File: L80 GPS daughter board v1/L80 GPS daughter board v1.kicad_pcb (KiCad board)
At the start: 4 copper layers, 29.8 x 35.1 mm, 13 parts, among them J1 Conn_01x06_Socket, SW1 SW_Push, U1 AP2112K-3.3, U2 L80-R, U3 MCP73831-2-OT

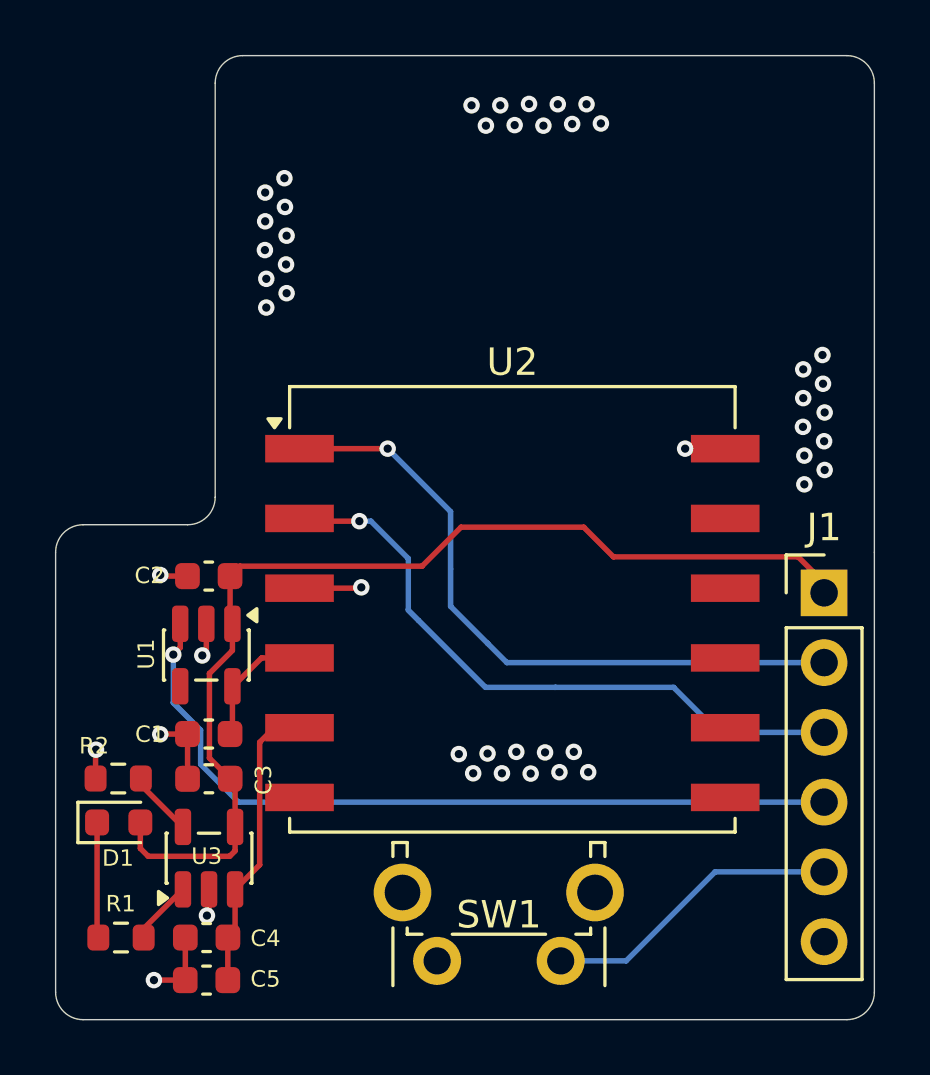
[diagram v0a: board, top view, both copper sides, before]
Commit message: modefied gps board to handle sdcard operations and power input
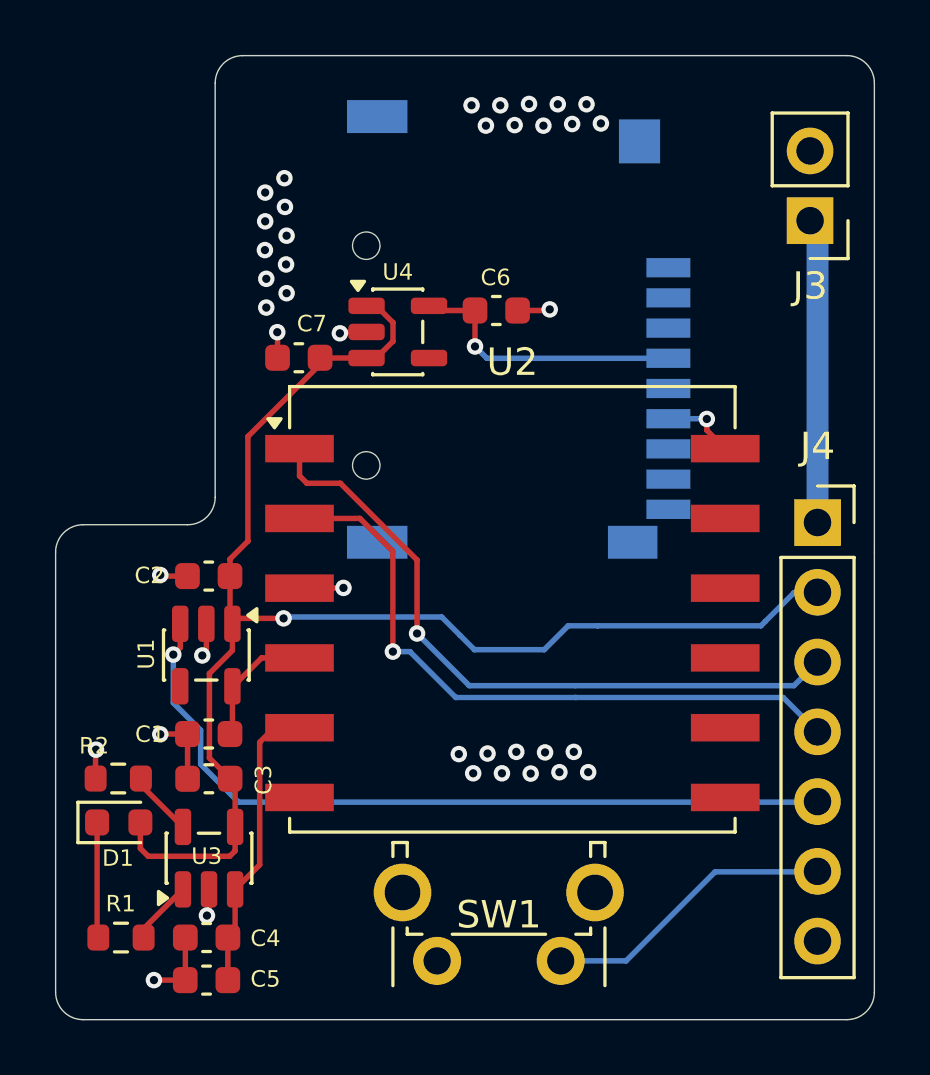
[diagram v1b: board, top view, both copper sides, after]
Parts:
- removed J1: Conn_01x06_Socket, Connector_PinHeader_2.54mm:PinHeader_1x06_P2.54mm_Vertical
- added C6: 1uF, Capacitor_SMD:C_0603_1608Metric, F.Cu at (133.2, 90.1)
- added C7: 1uF, Capacitor_SMD:C_0603_1608Metric, F.Cu at (126.0, 91.8)
- added J2: THD2528-11SD-GF, KiCad:THD252811SDGF, B.Cu at (131.7, 90.5)
- added J3: Conn_01x02_Pin, Connector_PinHeader_2.54mm:PinHeader_1x02_P2.54mm_Vertical, F.Cu at (144.6, 86.8)
- added J4: Conn_01x07_Socket, Connector_PinSocket_2.54mm:PinSocket_1x07_P2.54mm_Vertical, F.Cu at (144.9, 97.8)
- added U4: AP2112K-3.3, Package_TO_SOT_SMD:SOT-23-5, F.Cu at (129.6, 90.8)
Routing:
- net +5V: track 39.1 -> 52.5 mm, vias 0 -> 1
- net 5:32Vin: track 0.00 -> 11.1 mm
- net SD_CARD_PWR: track 0.00 -> 10.3 mm, vias 0 -> 1
- net GND: track 13.3 -> 17.1 mm, vias 48 -> 41
- net gps_tx: track 23.3 -> 24.4 mm
- net gps_rx: track 24.2 -> 24.9 mm

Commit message: added SD card pinout
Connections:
- J2 pad 2: unconnected-(J2-CD/DAT3-Pad2) -> SD_CS
- J2 pad 3: unconnected-(J2-CMD-Pad3) -> MOSI
- J2 pad 5: unconnected-(J2-CLX-Pad5) -> SCLK
- J2 pad 7: unconnected-(J2-DAT0-Pad7) -> MISO
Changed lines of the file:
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@@
 	(net 18 "stat")
 	(net 19 "SD_CARD_PWR")
-	(net 20 "unconnected-(J2-CMD-Pad3)")
+	(net 20 "MOSI")
 	(net 21 "unconnected-(J2-PadMP2)")
 	(net 22 "unconnected-(J2-DAT2-Pad1)")
-	(net 23 "unconnected-(J2-CD{slash}DAT3-Pad2)")
+	(net 23 "SD_CS")
 	(net 24 "unconnected-(J2-PadMP4)")
-	(net 25 "unconnected-(J2-DAT0-Pad7)")
+	(net 25 "MISO")
 	(net 26 "unconnected-(J2-PadMP1)")
 	(net 27 "unconnected-(J2-DAT1-Pad8)")
 	(net 28 "unconnected-(J2-CD-Pad9)")
 	(net 29 "unconnected-(J2-PadMP3)")
-	(net 30 "unconnected-(J2-CLX-Pad5)")
+	(net 30 "SCLK")
 	(net 31 "unconnected-(U4-NC-Pad4)")
 	(net 32 "5:32Vin")
@@
 			(net 22 "unconnected-(J2-DAT2-Pad1)")
 			(pinfunction "DAT2")
-			(pintype "passive")
+			(pintype "passive+no_connect")
 			(teardrops
 				(best_length_ratio 0.5)
@@
 			(size 0.7 1.6)
 			(layers "B.Cu" "B.Mask" "B.Paste")
-			(net 23 "unconnected-(J2-CD{slash}DAT3-Pad2)")
+			(net 23 "SD_CS")
 			(pinfunction "CD/DAT3")
 			(pintype "passive")
@@
 			(size 0.7 1.6)
 			(layers "B.Cu" "B.Mask" "B.Paste")
-			(net 20 "unconnected-(J2-CMD-Pad3)")
+			(net 20 "MOSI")
 			(pinfunction "CMD")
 			(pintype "passive")
@@
 			(size 0.7 1.6)
 			(layers "B.Cu" "B.Mask" "B.Paste")
-			(net 30 "unconnected-(J2-CLX-Pad5)")
+			(net 30 "SCLK")
 			(pinfunction "CLX")
 			(pintype "passive")
@@
 			(size 0.7 1.6)
 			(layers "B.Cu" "B.Mask" "B.Paste")
-			(net 25 "unconnected-(J2-DAT0-Pad7)")
+			(net 25 "MISO")
 			(pinfunction "DAT0")
 			(pintype "passive")
@@
 			(net 27 "unconnected-(J2-DAT1-Pad8)")
 			(pinfunction "DAT1")
-			(pintype "passive")
+			(pintype "passive+no_connect")
 			(teardrops
 				(best_length_ratio 0.5)
@@
 	)
 	(zone
-		(net 19)
-		(net_name "SD_CARD_PWR")
+		(net 5)
+		(net_name "gps_rx")
 		(layer "B.Cu")
 		(name "$teardrop_padvia$")
 		(hatch none 0.1)
-		(priority 30009)
+		(priority 30003)
 		(attr
 			(teardrop
@@
 		(polygon
 			(pts
-				(xy 138.28 91.71) (xy 138.28 91.91) (xy 138.63 92.16) (xy 139.431 91.81) (xy 138.63 91.46)
+				(xy 143.532556 103.63) (xy 143.532556 103.83) (xy 145.025827 103.703667) (xy 144.861 102.87) (xy 144.153251 102.397765)
 			)
 		)
 	)
 	(zone
-		(net 5)
-		(net_name "gps_rx")
+		(net 3)
+		(net_name "+5V")
 		(layer "B.Cu")
 		(name "$teardrop_padvia$")
 		(hatch none 0.1)
-		(priority 30003)
+		(priority 30015)
 		(attr
 			(teardrop
@@
 		(polygon
 			(pts
-				(xy 143.532556 103.63) (xy 143.532556 103.83) (xy 145.025827 103.703667) (xy 144.861 102.87) (xy 144.153251 102.397765)
+				(xy 126.014236 101.329) (xy 126.014236 101.129) (xy 125.478527 100.985764) (xy 125.419 101.28) (xy 125.586671 101.529441)
 			)
 		)
 	)
 	(zone
-		(net 3)
-		(net_name "+5V")
+		(net 7)
+		(net_name "PWR_SWITCH")
 		(layer "B.Cu")
 		(name "$teardrop_padvia$")
 		(hatch none 0.1)
-		(priority 30015)
+		(priority 30000)
 		(attr
 			(teardrop
@@
 		(polygon
 			(pts
-				(xy 126.014236 101.329) (xy 126.014236 101.129) (xy 125.478527 100.985764) (xy 125.419 101.28) (xy 125.586671 101.529441)
+				(xy 137.243187 113.85) (xy 137.243187 113.65) (xy 135.996124 113.022464) (xy 135.509 113.75) (xy 135.996124 114.477536)
 			)
 		)
@@
 		(name "$teardrop_padvia$")
 		(hatch none 0.1)
-		(priority 30002)
+		(priority 30004)
 		(attr
 			(teardrop
@@
 		(polygon
 			(pts
-				(xy 137.243187 113.85) (xy 137.243187 113.65) (xy 135.996124 113.022464) (xy 135.509 113.75) (xy 135.996124 114.477536)
+				(xy 143.176333 110.41) (xy 143.176333 110.61) (xy 144.387765 111.196749) (xy 144.861 110.49) (xy 144.387765 109.783251)
 			)
 		)
 	)
 	(zone
-		(net 7)
-		(net_name "PWR_SWITCH")
+		(net 1)
+		(net_name "GND")
 		(layer "B.Cu")
 		(name "$teardrop_padvia$")
 		(hatch none 0.1)
-		(priority 30004)
+		(priority 30001)
 		(attr
 			(teardrop
@@
 		(polygon
 			(pts
-				(xy 143.176333 110.41) (xy 143.176333 110.61) (xy 144.387765 111.196749) (xy 144.861 110.49) (xy 144.387765 109.783251)
+				(xy 140.58 94.11) (xy 140.58 93.91) (xy 140.23 93.66) (xy 139.429 94.01) (xy 140.23 94.36)
 			)
 		)
@@
 	)
 	(zone
-		(net 1)
-		(net_name "GND")
+		(net 6)
+		(net_name "GPS_Switch")
 		(layer "B.Cu")
 		(name "$teardrop_padvia$")
 		(hatch none 0.1)
-		(priority 30008)
+		(priority 30005)
 		(attr
 			(teardrop
@@
 		(polygon
 			(pts
-				(xy 140.58 94.11) (xy 140.58 93.91) (xy 140.23 93.66) (xy 139.429 94.01) (xy 140.23 94.36)
+				(xy 143.176333 107.87) (xy 143.176333 108.07) (xy 144.387765 108.656749) (xy 144.861 107.95) (xy 144.387765 107.243251)
 			)
 		)
 	)
 	(zone
-		(net 6)
-		(net_name "GPS_Switch")
+		(net 32)
+		(net_name "5:32Vin")
 		(layer "B.Cu")
 		(name "$teardrop_padvia$")
 		(hatch none 0.1)
-		(priority 30005)
+		(priority 30000)
 		(attr
 			(teardrop
@@
 		(polygon
 			(pts
-				(xy 143.176333 107.87) (xy 143.176333 108.07) (xy 144.387765 108.656749) (xy 144.861 107.95) (xy 144.387765 107.243251)
+				(xy 145.26 96.09) (xy 144.46 96.09) (xy 144.01 96.94) (xy 144.86 97.791) (xy 145.71 96.94)
 			)
 		)
 	)
 	(zone
-		(net 32)
-		(net_name "5:32Vin")
+		(net 4)
+		(net_name "gps_tx")
 		(layer "B.Cu")
 		(name "$teardrop_padvia$")
 		(hatch none 0.1)
-		(priority 30000)
+		(priority 30006)
 		(attr
 			(teardrop
@@
 		(polygon
 			(pts
-				(xy 145.26 96.09) (xy 144.46 96.09) (xy 144.01 96.94) (xy 144.86 97.791) (xy 145.71 96.94)
+				(xy 143.740178 104.148757) (xy 143.598757 104.290178) (xy 144.026333 105.575827) (xy 144.860707 105.410707)
+				(xy 145.025827 104.576333)
 			)
 		)
 	)
 	(zone
-		(net 4)
-		(net_name "gps_tx")
+		(net 3)
+		(net_name "+5V")
 		(layer "B.Cu")
 		(name "$teardrop_padvia$")
 		(hatch none 0.1)
-		(priority 30006)
+		(priority 30007)
 		(attr
 			(teardrop
@@
 		(polygon
 			(pts
-				(xy 143.740178 104.148757) (xy 143.598757 104.290178) (xy 144.026333 105.575827) (xy 144.860707 105.410707)
-				(xy 145.025827 104.576333)
+				(xy 143.346869 100.861709) (xy 143.488291 101.003131) (xy 144.694173 101.163667) (xy 144.860707 100.329293)
+				(xy 144.153251 99.857765)
 			)
 		)
 	)
 	(zone
-		(net 3)
-		(net_name "+5V")
+		(net 32)
+		(net_name "5:32Vin")
 		(layer "B.Cu")
 		(name "$teardrop_padvia$")
 		(hatch none 0.1)
-		(priority 30007)
+		(priority 30001)
 		(attr
 			(teardrop
@@
 		(polygon
 			(pts
-				(xy 143.346869 100.861709) (xy 143.488291 101.003131) (xy 144.694173 101.163667) (xy 144.860707 100.329293)
-				(xy 144.153251 99.857765)
+				(xy 144.46 88.5) (xy 145.26 88.5) (xy 145.44 87.65) (xy 144.59 86.799) (xy 143.864438 87.65)
 			)
 		)
 	)
 	(zone
-		(net 32)
-		(net_name "5:32Vin")
+		(net 19)
+		(net_name "SD_CARD_PWR")
 		(layer "B.Cu")
 		(name "$teardrop_padvia$")
 		(hatch none 0.1)
-		(priority 30001)
+		(priority 30002)
 		(attr
 			(teardrop
@@
 		(polygon
 			(pts
-				(xy 144.46 88.5) (xy 145.26 88.5) (xy 145.44 87.65) (xy 144.59 86.799) (xy 143.864438 87.65)
+				(xy 138.28 91.71) (xy 138.28 91.91) (xy 138.63 92.16) (xy 139.431 91.81) (xy 138.63 91.46)
 			)
 		)

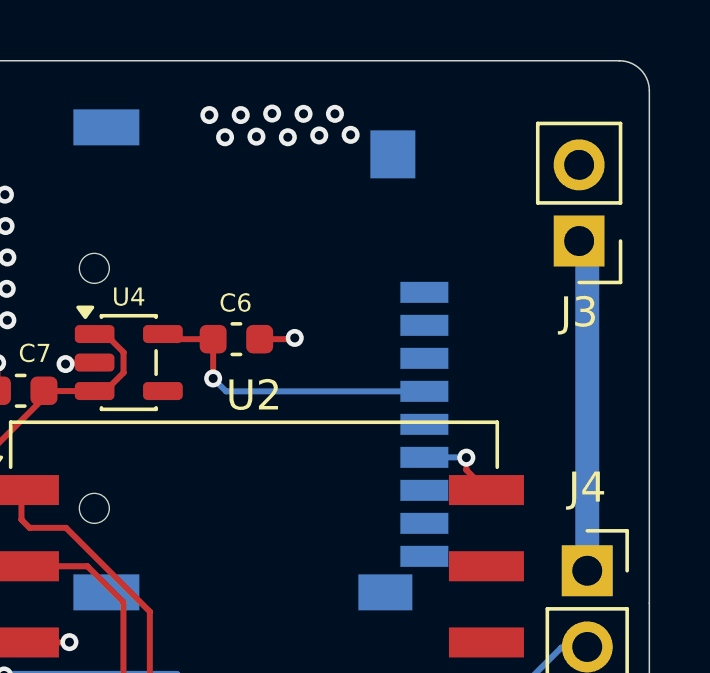
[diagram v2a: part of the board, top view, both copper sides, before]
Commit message: cleaned up sd card routing and added appropriate connectors
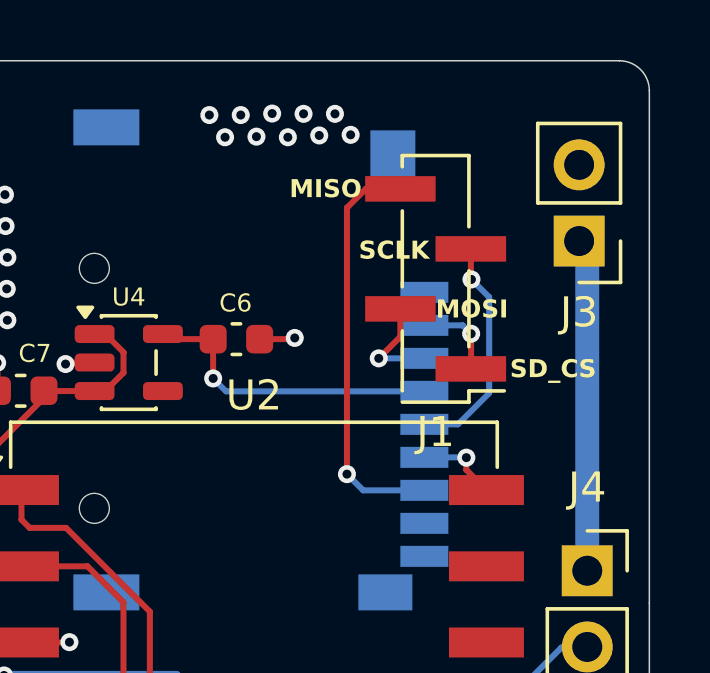
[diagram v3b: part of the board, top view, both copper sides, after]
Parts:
- added J1: Conn_01x04_Pin, Connector_PinHeader_2.00mm:PinHeader_1x04_P2.00mm_Vertical_SMD_Pin1Left, F.Cu at (139.8, 88.1)
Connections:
- net VBAT_RTC renamed VBAT_BACKUP
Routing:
- net MISO: track 0.00 -> 13.7 mm, vias 0 -> 1
- net SCLK: track 0.00 -> 7.65 mm, vias 0 -> 1
- net MOSI: track 0.00 -> 3.47 mm, vias 0 -> 1
- net SD_CS: track 0.00 -> 2.85 mm, vias 0 -> 1
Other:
- board text added: "MISO"
- board text added: "MOSI"
- board text added: "SCLK"
- board text added: "SD_CS"

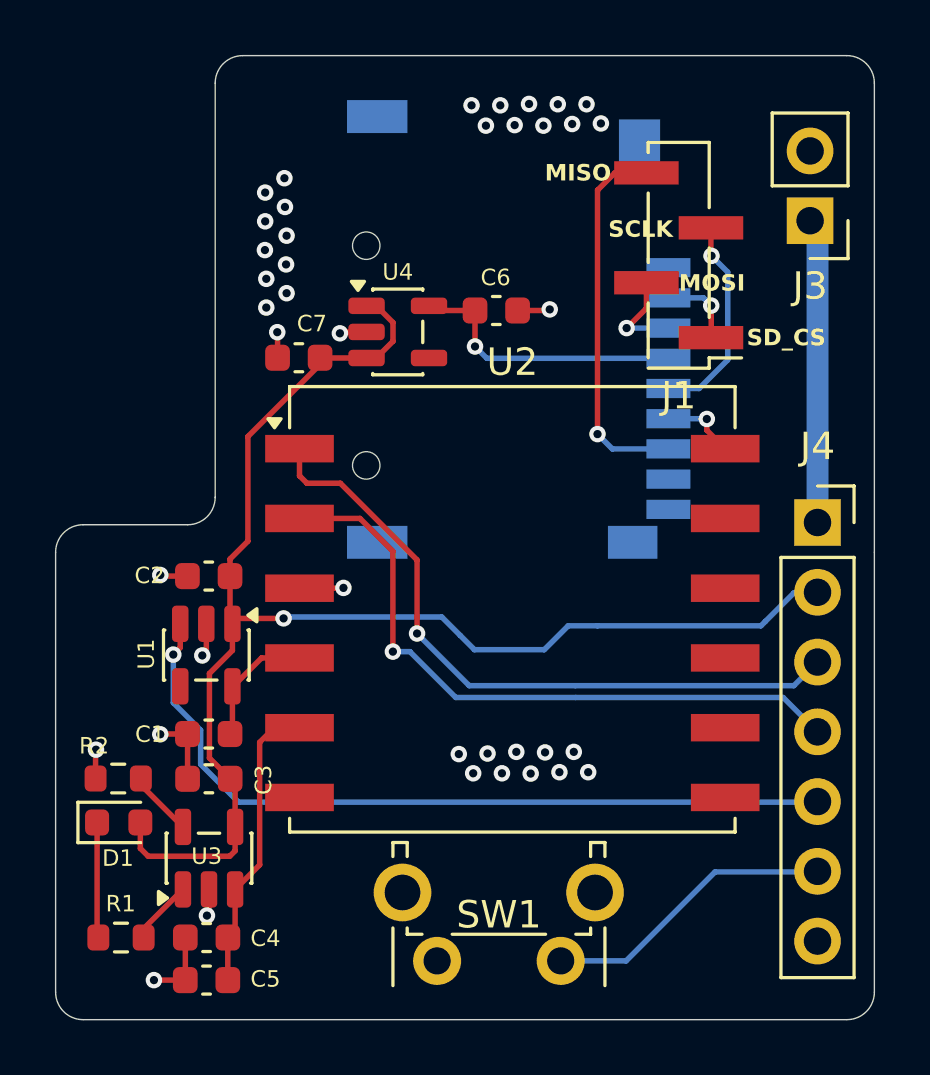
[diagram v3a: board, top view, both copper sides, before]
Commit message: modefied gps board pins
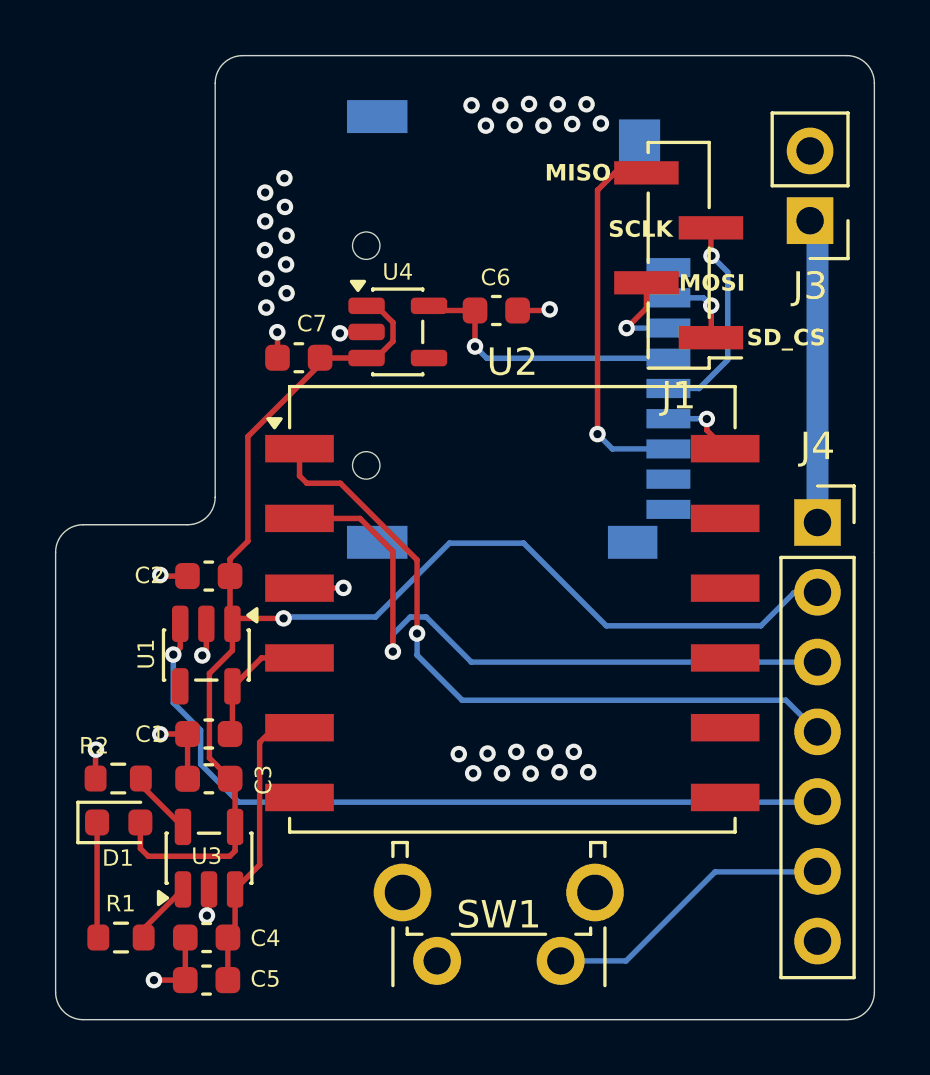
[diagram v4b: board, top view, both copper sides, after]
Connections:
- J4 pad 3: gps_rx -> gps_tx
- J4 pad 4: gps_tx -> gps_rx
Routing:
- net +5V: track 52.5 -> 54.0 mm
- net gps_rx: track 24.9 -> 25.7 mm
